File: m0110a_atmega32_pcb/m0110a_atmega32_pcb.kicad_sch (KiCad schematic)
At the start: 4 parts, among them J1 Conn_01x40_Pin, J2 ISP, J3 Serial, U2 ATmega32A-M

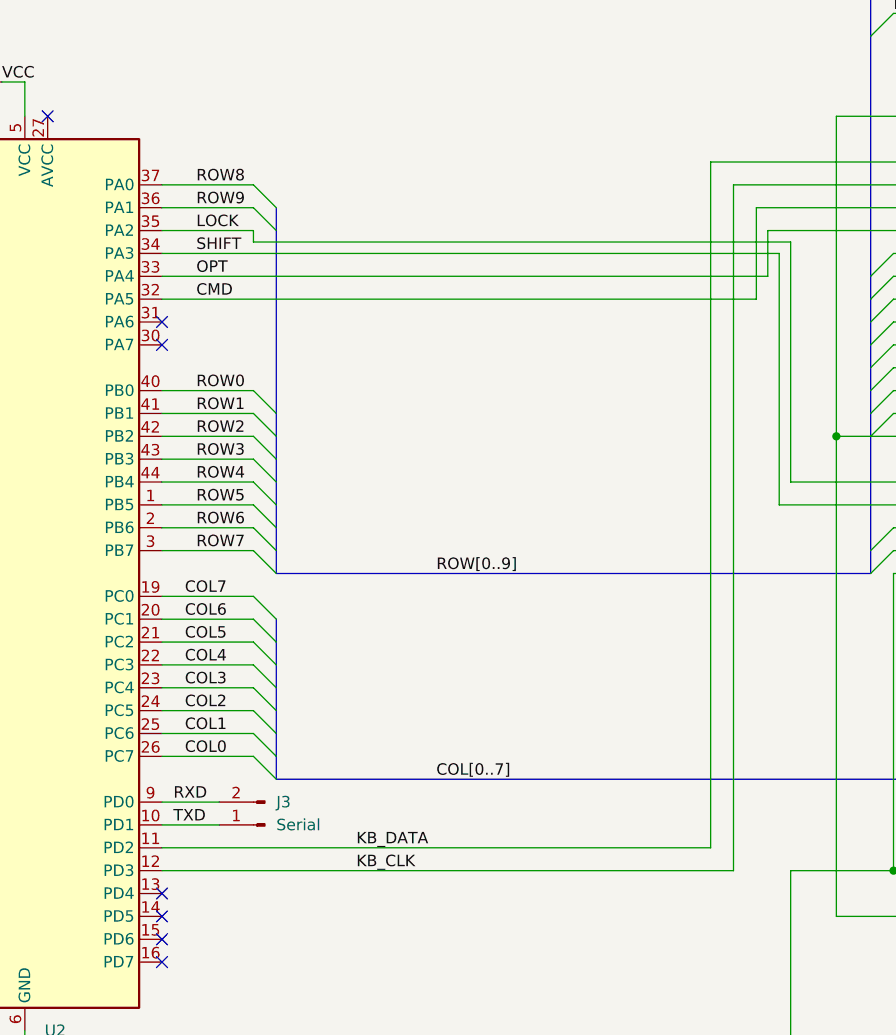
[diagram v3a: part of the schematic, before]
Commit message: Swapped data and clk for easier layout. V 2.1
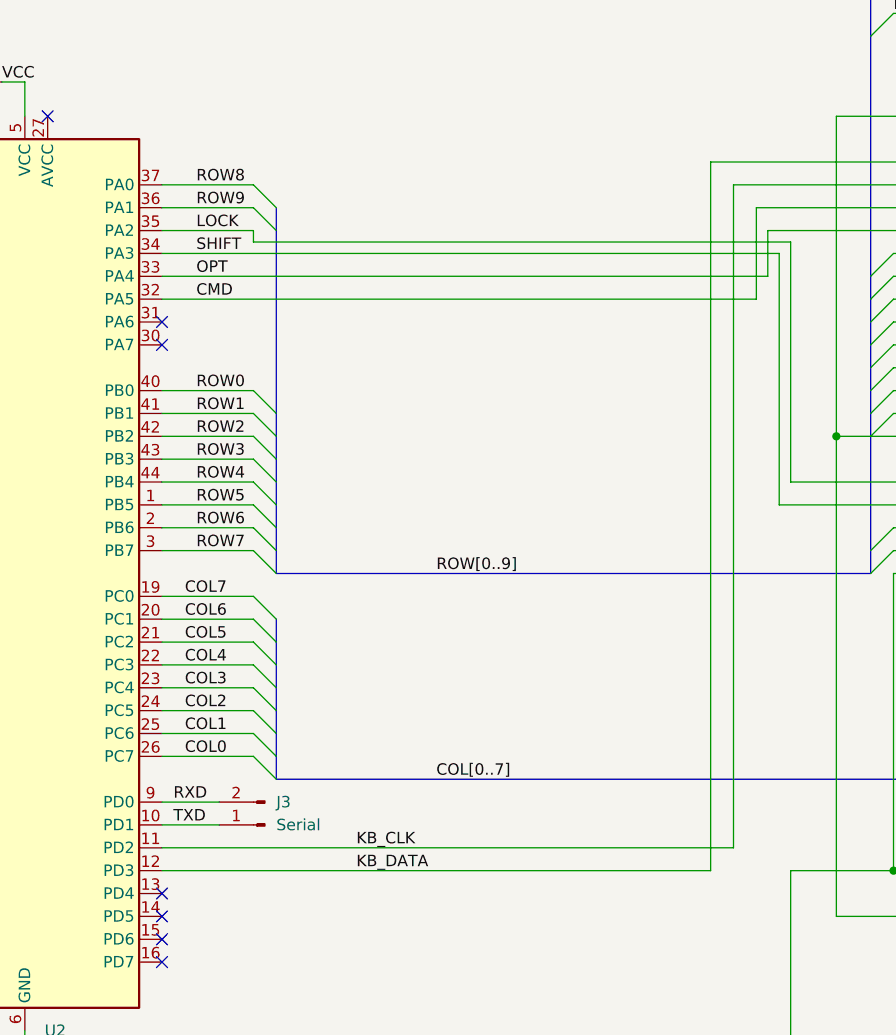
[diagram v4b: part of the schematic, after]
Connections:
- net KB_CLK: now also U2.11 (PD2); no longer U2.12 (PD3)
- net KB_DATA: now also U2.12 (PD3); no longer U2.11 (PD2)
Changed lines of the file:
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@@
-    (stroke (width 0) (type default))
-  )
-  (wire (pts (xy 118.11 129.54) (xy 181.61 129.54))
     (stroke (width 0) (type default))
   )
@@
     (stroke (width 0) (type default))
   )
-  (wire (pts (xy 118.11 127) (xy 179.07 127))
-    (stroke (width 0) (type default))
-  )
   (wire (pts (xy 118.11 124.46) (xy 124.46 124.46))
     (stroke (width 0) (type default))
@@
     (stroke (width 0) (type default))
   )
+  (wire (pts (xy 181.61 127) (xy 181.61 53.34))
+    (stroke (width 0) (type default))
+  )
   (bus (pts (xy 130.81 86.36) (xy 130.81 88.9))
     (stroke (width 0) (type default))
@@
     (stroke (width 0) (type default))
   )
-  (wire (pts (xy 179.07 127) (xy 179.07 50.8))
+  (wire (pts (xy 179.07 50.8) (xy 179.07 129.54))
     (stroke (width 0) (type default))
   )
@@
     (stroke (width 0) (type default))
   )
+  (wire (pts (xy 118.11 127) (xy 181.61 127))
+    (stroke (width 0) (type default))
+  )
   (wire (pts (xy 193.04 134.62) (xy 217.17 134.62))
     (stroke (width 0) (type default))
@@
     (stroke (width 0) (type default))
   )
+  (wire (pts (xy 118.11 129.54) (xy 179.07 129.54))
+    (stroke (width 0) (type default))
+  )
   (wire (pts (xy 199.39 63.5) (xy 217.17 63.5))
     (stroke (width 0) (type default))
@@
     (stroke (width 0) (type default))
   )
-  (wire (pts (xy 181.61 129.54) (xy 181.61 53.34))
-    (stroke (width 0) (type default))
-  )
   (wire (pts (xy 193.04 81.28) (xy 193.04 45.72))
     (stroke (width 0) (type default))
@@
     (effects (font (size 1.27 1.27)) (justify left bottom))
   )
-  (label "KB_CLK" (at 139.7 129.54 0) (fields_autoplaced)
+  (label "KB_DATA" (at 139.7 129.54 0) (fields_autoplaced)
     (effects (font (size 1.27 1.27)) (justify left bottom))
   )
@@
     (effects (font (size 1.27 1.27)) (justify left bottom))
   )
-  (label "KB_DATA" (at 139.7 127 0) (fields_autoplaced)
-    (effects (font (size 1.27 1.27)) (justify left bottom))
-  )
+  (label "KB_CLK" (at 139.7 127 0) (fields_autoplaced)
+    (effects (font (size 1.27 1.27)) (justify left bottom))
+  )
